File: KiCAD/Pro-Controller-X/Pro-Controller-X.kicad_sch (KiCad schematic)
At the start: 91 parts, among them J2 CONN_02PTH2, J2 USB_C_Receptacle_USB2.0, Q1 2N7002, Q2 2N7002, Q3 2N7002, Q4 2N7002, Q5 2N7002, Q6 2N7002, Q7 2N7002, Q8 2N7002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

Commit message: More routing completed
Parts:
- J2: footprint 1X02_BIG -> Connector_PinHeader_2.54mm:PinHeader_1x02_P2.54mm_Vertical
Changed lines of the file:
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@@
       (effects (font (size 1.143 1.143)))
     )
-    (property "Footprint" "1X02_BIG" (at 375.92 100.33 0)
+    (property "Footprint" "Connector_PinHeader_2.54mm:PinHeader_1x02_P2.54mm_Vertical" (at 375.92 100.33 0)
       (effects (font (size 0.508 0.508)) hide)
     )

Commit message: Most traces routed
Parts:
- Q2, Q3, Q5: footprint Package_TO_SOT_SMD:SOT-23 -> Package_TO_SOT_SMD:TSOT-23
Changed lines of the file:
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@@
       (effects (font (size 1.27 1.27)))
     )
-    (property "Footprint" "Package_TO_SOT_SMD:SOT-23" (at 182.245 137.16 0)
+    (property "Footprint" "Package_TO_SOT_SMD:TSOT-23" (at 182.245 137.16 0)
       (effects (font (size 1.27 1.27) italic) (justify left) hide)
     )
@@
       (effects (font (size 1.27 1.27)) (justify left))
     )
-    (property "Footprint" "Package_TO_SOT_SMD:SOT-23" (at 156.21 155.575 0)
+    (property "Footprint" "Package_TO_SOT_SMD:TSOT-23" (at 156.21 155.575 0)
       (effects (font (size 1.27 1.27) italic) (justify left) hide)
     )
@@
       (effects (font (size 1.27 1.27)) (justify left))
     )
-    (property "Footprint" "Package_TO_SOT_SMD:SOT-23" (at 167.64 184.785 0)
+    (property "Footprint" "Package_TO_SOT_SMD:TSOT-23" (at 167.64 184.785 0)
       (effects (font (size 1.27 1.27) italic) (justify left) hide)
     )

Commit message: Copper Pours complete, via stitching started
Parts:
- added J4: CONN_04, Connector_PinHeader_1.27mm:PinHeader_1x04_P1.27mm_Vertical, symbol SparkFun-Connectors:CONN_04
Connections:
- net GND: now also U5.6, U5.7, J4.4
- net V_BATT: now also J4.1
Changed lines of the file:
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@@
   (junction (at 248.92 40.64) (diameter 0) (color 0 0 0 0)
   )
+  (junction (at 297.18 205.74) (diameter 0) (color 0 0 0 0)
+  )
   (junction (at 165.1 195.58) (diameter 0) (color 0 0 0 0)
   )
@@
   (junction (at 308.61 245.11) (diameter 0) (color 0 0 0 0)
   )
+  (junction (at 294.64 205.74) (diameter 0) (color 0 0 0 0)
+  )
   (junction (at 170.18 208.28) (diameter 0) (color 0 0 0 0)
   )
@@
     (stroke (width 0) (type default))
   )
+  (wire (pts (xy 358.14 208.28) (xy 358.14 209.55))
+    (stroke (width 0) (type default))
+  )
   (wire (pts (xy 60.96 77.47) (xy 64.77 77.47))
     (stroke (width 0) (type default))
@@
     (stroke (width 0) (type default))
   )
+  (wire (pts (xy 294.64 205.74) (xy 294.64 207.01))
+    (stroke (width 0) (type default))
+  )
   (wire (pts (xy 200.66 149.86) (xy 201.93 149.86))
     (stroke (width 0) (type default))
@@
     (stroke (width 0) (type default))
   )
+  (wire (pts (xy 297.18 205.74) (xy 294.64 205.74))
+    (stroke (width 0) (type default))
+  )
   (wire (pts (xy 189.23 195.58) (xy 200.66 195.58))
     (stroke (width 0) (type default))
   )
+  (wire (pts (xy 358.14 199.39) (xy 358.14 200.66))
+    (stroke (width 0) (type default))
+  )
   (wire (pts (xy 35.56 67.31) (xy 46.99 67.31))
     (stroke (width 0) (type default))
@@
     (stroke (width 0) (type default))
   )
-  (wire (pts (xy 294.64 204.47) (xy 294.64 207.01))
+  (wire (pts (xy 294.64 204.47) (xy 294.64 205.74))
     (stroke (width 0) (type default))
   )
@@
     (stroke (width 0) (type default))
   )
+  (wire (pts (xy 358.14 200.66) (xy 359.41 200.66))
+    (stroke (width 0) (type default))
+  )
   (wire (pts (xy 168.91 219.71) (xy 168.91 220.98))
     (stroke (width 0) (type default))
   )
+  (wire (pts (xy 299.72 205.74) (xy 297.18 205.74))
+    (stroke (width 0) (type default))
+  )
   (wire (pts (xy 193.04 165.1) (xy 193.04 182.88))
     (stroke (width 0) (type default))
@@
     (stroke (width 0) (type default))
   )
+  (wire (pts (xy 297.18 191.77) (xy 297.18 205.74))
+    (stroke (width 0) (type default))
+  )
   (wire (pts (xy 485.14 92.71) (xy 487.68 92.71))
     (stroke (width 0) (type default))
@@
     (stroke (width 0) (type default))
   )
+  (wire (pts (xy 359.41 208.28) (xy 358.14 208.28))
+    (stroke (width 0) (type default))
+  )
   (wire (pts (xy 389.89 137.16) (xy 393.7 137.16))
     (stroke (width 0) (type default))
@@
     (stroke (width 0) (type default))
   )
+  (wire (pts (xy 299.72 191.77) (xy 299.72 205.74))
+    (stroke (width 0) (type default))
+  )
   (wire (pts (xy 369.57 231.14) (xy 369.57 233.68))
     (stroke (width 0) (type default))
@@
     )
   )
+  (symbol (lib_id "power:GND") (at 358.14 209.55 0) (unit 1)
+    (in_bom yes) (on_board yes) (dnp no) (fields_autoplaced)
+    (property "Reference" "#PWR041" (at 358.14 215.9 0)
+      (effects (font (size 1.27 1.27)) hide)
+    )
+    (property "Value" "GND" (at 358.14 214.63 0)
+      (effects (font (size 1.27 1.27)))
+    )
+    (property "Footprint" "" (at 358.14 209.55 0)
+      (effects (font (size 1.27 1.27)) hide)
+    )
+    (property "Datasheet" "" (at 358.14 209.55 0)
+      (effects (font (size 1.27 1.27)) hide)
+    )
+    (pin "1")
+    (instances
+      (project "Pro-Controller-X"
+        (path "/40a7657d-c4d7-4ebc-b606-0c6932d6f433"
+          (reference "#PWR041") (unit 1)
+        )
+      )
+    )
+  )
   (symbol (lib_id "Device:R_US") (at 458.47 168.91 270) (unit 1)
     (in_bom yes) (on_board yes) (dnp no)
@@
     )
   )
+  (symbol (lib_id "SparkFun-Connectors:CONN_04") (at 361.95 200.66 180) (unit 1)
+    (in_bom yes) (on_board yes) (dnp no) (fields_autoplaced)
+    (property "Reference" "J4" (at 368.3 201.93 0)
+      (effects (font (size 1.143 1.143)) (justify right))
+    )
+    (property "Value" "CONN_04" (at 368.3 204.47 0)
+      (effects (font (size 1.143 1.143)) (justify right))
+    )
+    (property "Footprint" "Connector_PinHeader_1.27mm:PinHeader_1x04_P1.27mm_Vertical" (at 361.95 213.36 0)
+      (effects (font (size 0.508 0.508)) hide)
+    )
+    (property "Datasheet" "" (at 361.95 200.66 0)
+      (effects (font (size 1.27 1.27)) hide)
+    )
+    (property "unknown" "CONN-09696" (at 368.3 207.01 0)
+      (effects (font (size 1.524 1.524)) (justify right))
+    )
+    (pin "1")
+    (pin "2")
+    (pin "3")
+    (pin "4")
+    (instances
+      (project "Pro-Controller-X"
+        (path "/40a7657d-c4d7-4ebc-b606-0c6932d6f433"
+          (reference "J4") (unit 1)
+        )
+      )
+    )
+  )
   (symbol (lib_id "Device:C") (at 397.51 129.54 90) (unit 1)
     (in_bom yes) (on_board yes) (dnp no)
@@
         )
       )
+    )
+  )
+  (symbol (lib_id "SparkFun-PowerSymbols:V_BATT") (at 358.14 199.39 0) (unit 1)
+    (in_bom yes) (on_board yes) (dnp no)
+    (property "Reference" "#SUPPLY02" (at 359.41 199.39 0)
+      (effects (font (size 1.143 1.143)) (justify left bottom) hide)
+    )
+    (property "Value" "V_BATT" (at 358.14 195.58 0)
+      (effects (font (size 1.143 1.143)))
+    )
+    (property "Footprint" "XXX-00000" (at 358.14 194.31 0)
+      (effects (font (size 1.524 1.524)) hide)
+    )
+    (property "Datasheet" "" (at 358.14 199.39 0)
+      (effects (font (size 1.524 1.524)) hide)
+    )
+    (pin "~")
+    (instances
+      (project "Pro-Controller-X"
+        (path "/40a7657d-c4d7-4ebc-b606-0c6932d6f433"
+          (reference "#SUPPLY02") (unit 1)
+        )
+      )

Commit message: Test Gerber - Incomplete - Do Not Use
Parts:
- added JP1: SolderJumper_2_Bridged, Jumper:SolderJumper-2_P1.3mm_Bridged_RoundedPad1.0x1.5mm, symbol Jumper:SolderJumper_2_Bridged
- J4: footprint Connector_PinHeader_1.27mm:PinHeader_1x04_P1.27mm_Vertical -> Connector_PinHeader_2.00mm:PinHeader_1x04_P2.00mm_Vertical
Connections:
- net GND: now also JP1.1 (A)
- net at U6.22 (Mode_Sw): now also JP1.2 (B)
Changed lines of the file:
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@@
     (stroke (width 0) (type default))
   )
+  (wire (pts (xy 457.2 142.24) (xy 457.2 139.7))
+    (stroke (width 0) (type default))
+  )
   (wire (pts (xy 35.56 102.87) (xy 46.99 102.87))
     (stroke (width 0) (type default))
@@
     (stroke (width 0) (type default))
   )
+  (wire (pts (xy 467.36 139.7) (xy 487.68 139.7))
+    (stroke (width 0) (type default))
+  )
   (wire (pts (xy 231.14 40.64) (xy 237.49 40.64))
     (stroke (width 0) (type default))
@@
     (stroke (width 0) (type default))
   )
+  (wire (pts (xy 457.2 139.7) (xy 459.74 139.7))
+    (stroke (width 0) (type default))
+  )
   (wire (pts (xy 471.17 162.56) (xy 473.71 162.56))
     (stroke (width 0) (type default))
@@
     )
   )
+  (symbol (lib_id "Jumper:SolderJumper_2_Bridged") (at 463.55 139.7 0) (unit 1)
+    (in_bom yes) (on_board yes) (dnp no) (fields_autoplaced)
+    (property "Reference" "JP1" (at 463.55 133.35 0)
+      (effects (font (size 1.27 1.27)))
+    )
+    (property "Value" "SolderJumper_2_Bridged" (at 463.55 135.89 0)
+      (effects (font (size 1.27 1.27)))
+    )
+    (property "Footprint" "Jumper:SolderJumper-2_P1.3mm_Bridged_RoundedPad1.0x1.5mm" (at 463.55 139.7 0)
+      (effects (font (size 1.27 1.27)) hide)
+    )
+    (property "Datasheet" "~" (at 463.55 139.7 0)
+      (effects (font (size 1.27 1.27)) hide)
+    )
+    (pin "1")
+    (pin "2")
+    (instances
+      (project "Pro-Controller-X"
+        (path "/40a7657d-c4d7-4ebc-b606-0c6932d6f433"
+          (reference "JP1") (unit 1)
+        )
+      )
+    )
+  )
   (symbol (lib_id "Device:LED") (at 459.74 118.11 0) (unit 1)
     (in_bom yes) (on_board yes) (dnp no) (fields_autoplaced)
@@
     )
   )
+  (symbol (lib_id "power:GND") (at 457.2 142.24 0) (unit 1)
+    (in_bom yes) (on_board yes) (dnp no) (fields_autoplaced)
+    (property "Reference" "#PWR042" (at 457.2 148.59 0)
+      (effects (font (size 1.27 1.27)) hide)
+    )
+    (property "Value" "GND" (at 457.2 147.32 0)
+      (effects (font (size 1.27 1.27)))
+    )
+    (property "Footprint" "" (at 457.2 142.24 0)
+      (effects (font (size 1.27 1.27)) hide)
+    )
+    (property "Datasheet" "" (at 457.2 142.24 0)
+      (effects (font (size 1.27 1.27)) hide)
+    )
+    (pin "1")
+    (instances
+      (project "Pro-Controller-X"
+        (path "/40a7657d-c4d7-4ebc-b606-0c6932d6f433"
+          (reference "#PWR042") (unit 1)
+        )
+      )
+    )
+  )
   (symbol (lib_id "Device:C") (at 351.79 248.92 0) (unit 1)
     (in_bom yes) (on_board yes) (dnp no)
@@
       (effects (font (size 1.143 1.143)) (justify right))
     )
-    (property "Footprint" "Connector_PinHeader_1.27mm:PinHeader_1x04_P1.27mm_Vertical" (at 361.95 213.36 0)
+    (property "Footprint" "Connector_PinHeader_2.00mm:PinHeader_1x04_P2.00mm_Vertical" (at 361.95 213.36 0)
       (effects (font (size 0.508 0.508)) hide)
     )

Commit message: Missed pin from Rumble
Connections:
- net RMBL+: now also C8.2, U4.5
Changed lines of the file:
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@@
   (junction (at 224.79 82.55) (diameter 0) (color 0 0 0 0)
   )
+  (junction (at 189.23 204.47) (diameter 0) (color 0 0 0 0)
+  )
   (junction (at 317.5 168.91) (diameter 0) (color 0 0 0 0)
   )
@@
   )
   (wire (pts (xy 457.2 142.24) (xy 457.2 139.7))
+    (stroke (width 0) (type default))
+  )
+  (wire (pts (xy 189.23 204.47) (xy 193.04 204.47))
     (stroke (width 0) (type default))
   )
@@
       (effects (font (size 1.27 1.27)) (justify left) hide)
     )
+  )
+  (global_label "RMBL+" (shape input) (at 193.04 204.47 0) (fields_autoplaced)
+    (effects (font (size 1.27 1.27)) (justify left))
+    (property "Intersheetrefs" "${INTERSHEET_REFS}" (at 202.5377 204.47 0)
+      (effects (font (size 1.27 1.27)) (justify left) hide)
+    )

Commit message: Labeled Schematics and added Notes
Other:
- note added: "1.0.0"
- note added: "8BitDo Daughterboard Pinout"
- note added: "Appears to set the voltage for the Joysticks"
- note added: "Battery Connector"
- note added: "Gyro Control Circuit (Presumed)"
- note added: "Joystick Caps - Likely to provide stability and prevent snapback"
- note added: "Notes: - Transistors are likely the wrong type - Footprint was mapped correctly - Direction/type was not investigated - Circuit is attempted to be divided into sections - These sections will have notes on assumptions - Assumptions may not be correct, correct schematics was prioritized over understanding"
- note added: "Presumably this circuit is the voltage regulator circuit - No info could be found on regulators - Bothr egulators appear to regulate to the same voltage - Likely divided so that the Rumble motor doesn't affect the stability of the rest of the circuit"
- note added: "Pro Controller X"
- note added: "Pull-up for Charge Enable"
- note added: "Rumble Circuit"
- note added: "Seemingly part of the circuit is used to wake the controller and Switch when the home button is pressed, also sends back control to MCU"
- note added: "TP4056 Charging Circuit"
- note added: "USB/Power Input"
- note added: "Wii U Pro Controller Footprint - X1/Y1 is the Right Joystick - X2/Y2 is the Left Joystick - Resistors added to joystick voltage to set proper limits"
- moved on the sheet: C1, C13, C14, C15, C18, C19, C2, C20, C21, C3, C4, D1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

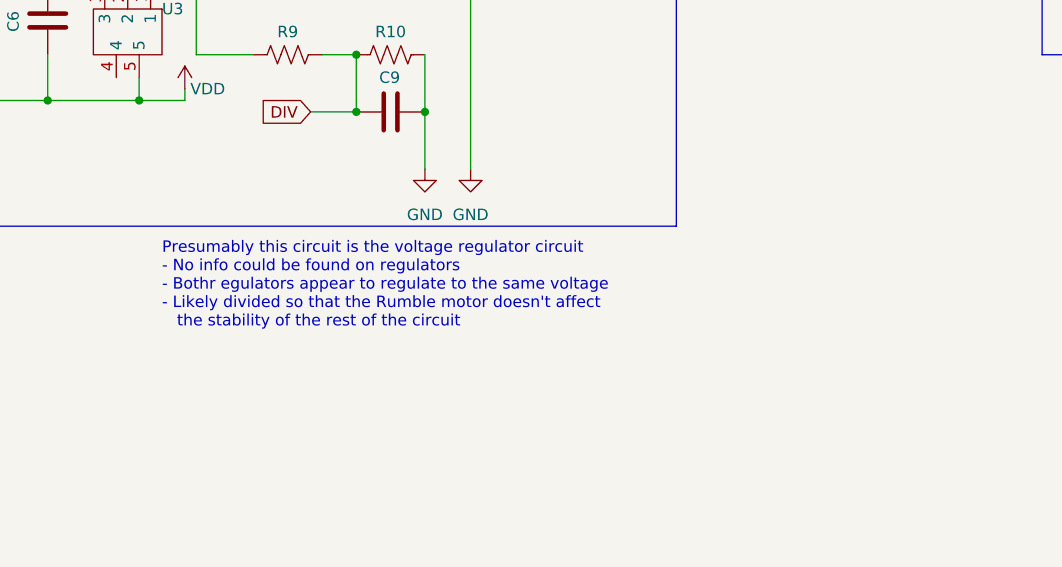
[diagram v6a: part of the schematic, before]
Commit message: Updated Labels on Schematics
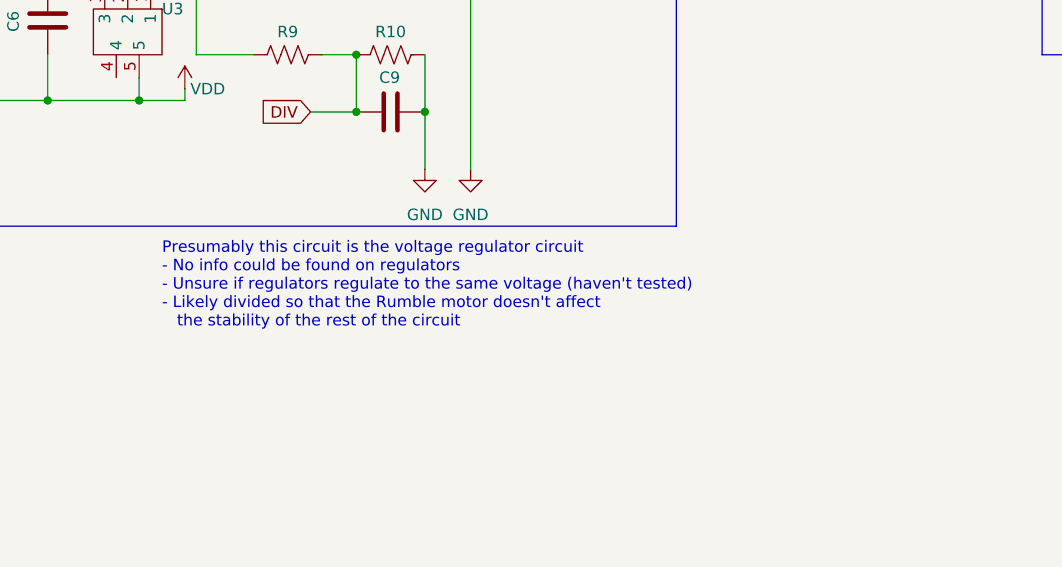
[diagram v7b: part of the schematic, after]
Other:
- note added: "Presumably this circuit is the voltage regulator circuit - No info could be found on regulators - Unsure if regulators regulate to the same voltage (haven't tested) - Likely divided so that the Rumble motor doesn't affect the stability of the rest of the circuit"
- note removed: "Presumably this circuit is the voltage regulator circuit - No info could be found on regulators - Bothr egulators appear to regulate to the same voltage - Likely divided so that the Rumble motor doesn't affect the stability of the rest of the circuit"
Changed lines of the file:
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@@
     (effects (font (size 1.27 1.27)) (justify left bottom))
   )
-  (text "Presumably this circuit is the voltage regulator circuit\n- No info could be found on regulators\n- Bothr egulators appear to regulate to the same voltage\n- Likely divided so that the Rumble motor doesn't affect\n   the stability of the rest of the circuit"
+  (text "Presumably this circuit is the voltage regulator circuit\n- No info could be found on regulators\n- Unsure if regulators regulate to the same voltage (haven't tested)\n- Likely divided so that the Rumble motor doesn't affect\n   the stability of the rest of the circuit"
     (at 166.37 246.38 0)
     (effects (font (size 1.27 1.27)) (justify left bottom))

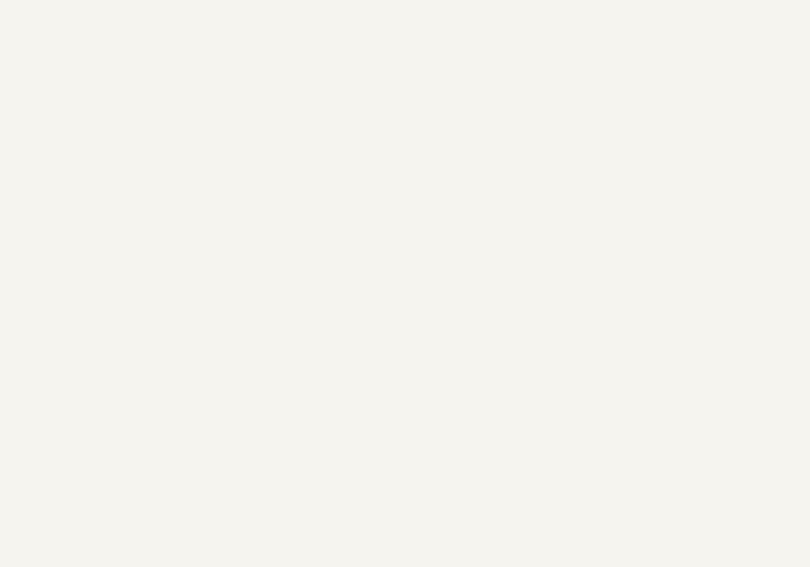
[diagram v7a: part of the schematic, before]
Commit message: Finished Routing and Stitching, Added Silkscreen
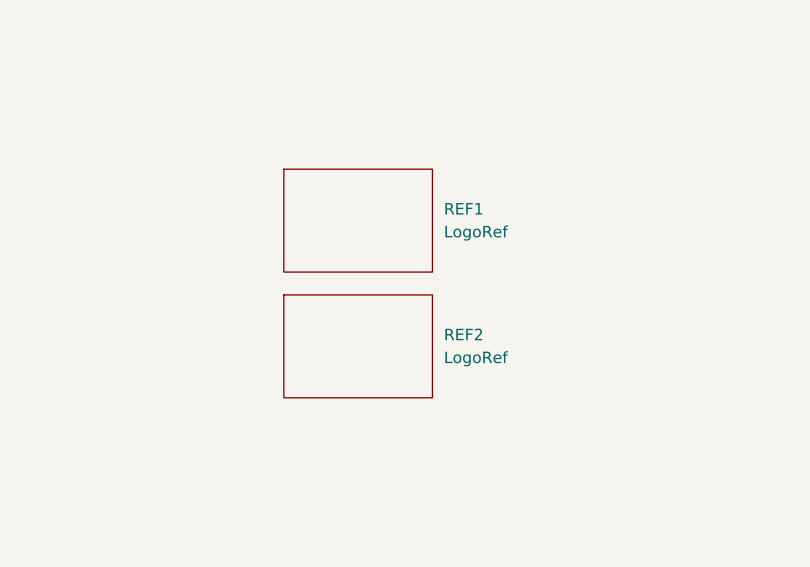
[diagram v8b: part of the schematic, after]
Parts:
- added REF1: LogoRef, A CustomLib:LegoRocketLogo15mm, symbol DSBB:LogoRef
- added REF2: LogoRef, A CustomLib:Linktree10mm, symbol DSBB:LogoRef
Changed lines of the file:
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@@
+    )
+  )
+  (symbol (lib_id "DSBB:LogoRef") (at 448.31 259.08 0) (unit 1)
+    (in_bom yes) (on_board yes) (dnp no) (fields_autoplaced)
+    (property "Reference" "REF2" (at 458.47 258.445 0)
+      (effects (font (size 1.27 1.27)) (justify left))
+    )
+    (property "Value" "LogoRef" (at 458.47 260.985 0)
+      (effects (font (size 1.27 1.27)) (justify left))
+    )
+    (property "Footprint" "A CustomLib:Linktree10mm" (at 448.31 259.08 0)
+      (effects (font (size 1.27 1.27)) hide)
+    )
+    (property "Datasheet" "" (at 448.31 259.08 0)
+      (effects (font (size 1.27 1.27)) hide)
+    )
+    (instances
+      (project "Pro-Controller-X"
+        (path "/40a7657d-c4d7-4ebc-b606-0c6932d6f433"
+          (reference "REF2") (unit 1)
+        )
+      )
     )
   )
@@
         )
       )
+    )
+  )
+  (symbol (lib_id "DSBB:LogoRef") (at 448.31 245.11 0) (unit 1)
+    (in_bom yes) (on_board yes) (dnp no) (fields_autoplaced)
+    (property "Reference" "REF1" (at 458.47 244.475 0)
+      (effects (font (size 1.27 1.27)) (justify left))
+    )
+    (property "Value" "LogoRef" (at 458.47 247.015 0)
+      (effects (font (size 1.27 1.27)) (justify left))
+    )
+    (property "Footprint" "A CustomLib:LegoRocketLogo15mm" (at 448.31 245.11 0)
+      (effects (font (size 1.27 1.27)) hide)
+    )
+    (property "Datasheet" "" (at 448.31 245.11 0)
+      (effects (font (size 1.27 1.27)) hide)
+    )
+    (instances
+      (project "Pro-Controller-X"
+        (path "/40a7657d-c4d7-4ebc-b606-0c6932d6f433"
+          (reference "REF1") (unit 1)
+        )
+      )
